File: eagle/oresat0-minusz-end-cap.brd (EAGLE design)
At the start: 106 x 106 mm, 30 parts, among them U1 LTC4305, U2 MMC5883MA, U3 MMC5883MA

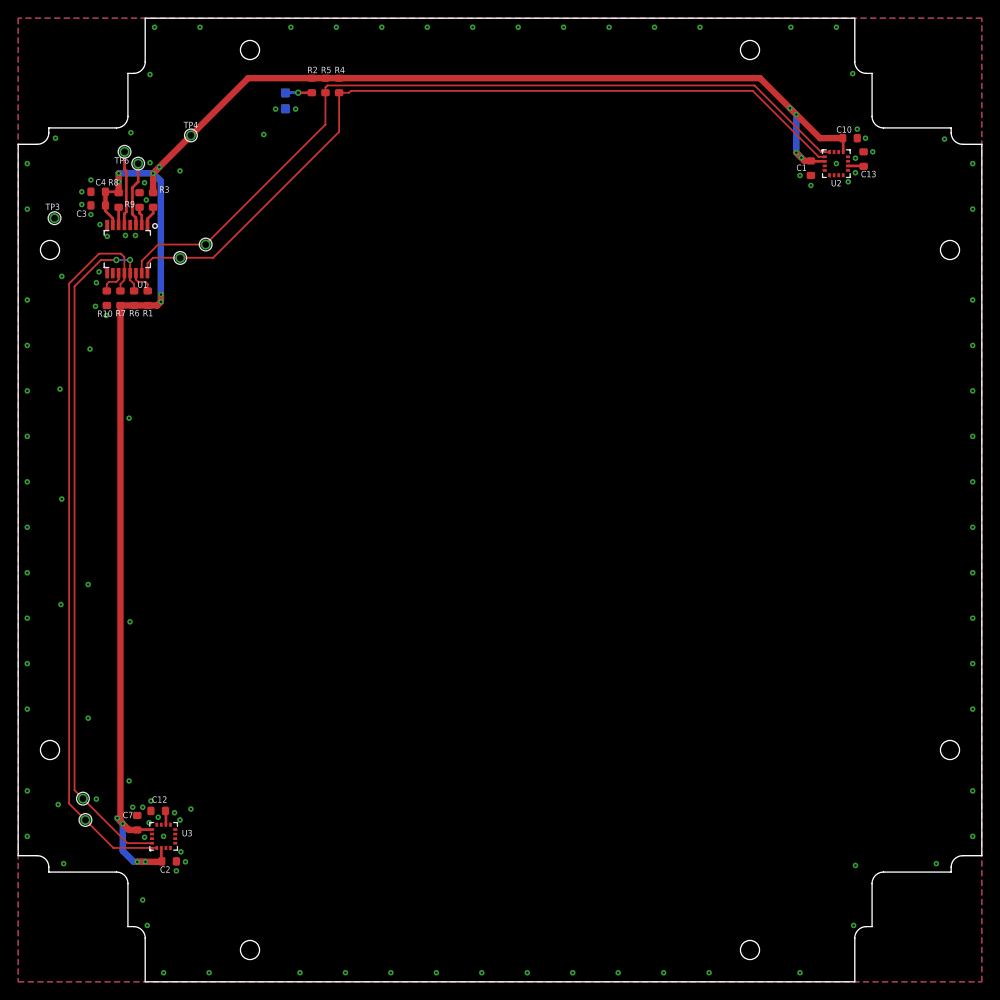
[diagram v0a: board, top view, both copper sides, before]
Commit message: Added connector to backplane. Added NP resistors connecting magnetometer interrupts to i2c buffer alert inputs. Moved traces out of bstop area, and moved components away from the backplane. Changed bus buffer i2c address. Added ground plane stitching, and fixed sharp edges on board outline.
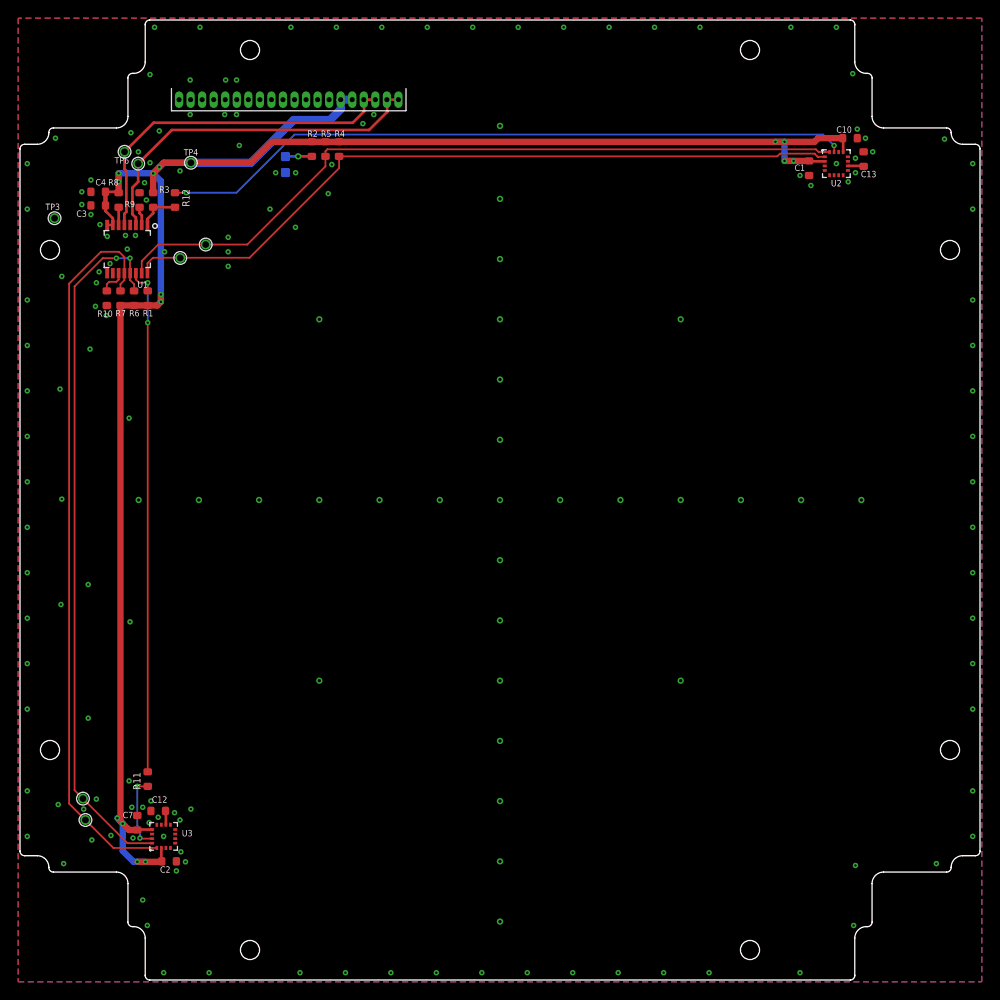
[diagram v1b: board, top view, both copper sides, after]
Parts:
- added J1: 6-104178-1, J-TE-6-104178-1-1.27mm-male-th:6-104178-1
- added R11, R12: NP, oresat-rcl:.0603-B-NOSILK
- moved D2 7.00 mm to (29.4, 89.9)
- moved R2 7.00 mm to (32.3, 91.6)
- moved R4 7.00 mm to (35.3, 91.6)
- moved R5 7.00 mm to (33.8, 91.6)
- moved TP4 3.00 mm to (19.0, 90.1)
- moved C1 0.20 mm to (87.0, 89.5)
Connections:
- new net !SD: J1.1
- new net CAN1_H: J1.4
- new net CAN1_L: J1.3
- new net CAN2_H: J1.9
- new net CAN2_L: J1.8
- new net N$10: R12.1, U2.15
- new net N$8: R11.1, U3.15
- new net OPD_PWR: J1.10
- new net OPD_SCL: J1.11
- new net OPD_SDA: J1.12
- new net SPARE1-TURNSTYLE-DPLY: J1.13
- new net SPARE2: J1.14
- new net VBUS: J1.7
- net 3.3V: now also J1.15, J1.16, U1.8
- net GND: now also J1.2, J1.5, J1.6; no longer U1.8
- net I2C-SCL: now also J1.17, J1.18
- net I2C-SDA: now also J1.19, J1.20
- net N$3: now also R11.2
- net N$4: now also R12.2
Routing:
- net N$10: track 0.00 -> 76.4 mm, vias 0 -> 2
- net N$3: track 2.95 -> 56.8 mm, vias 0 -> 2
- net I2C-SDA: track 7.16 -> 39.5 mm
- net I2C-SCL: track 8.22 -> 39.0 mm
- net 3.3V: track 201.0 -> 220.2 mm
- net N$8: track 0.00 -> 8.32 mm, vias 0 -> 2
- net SCL2: track 89.0 -> 81.5 mm
- net SDA2: track 90.5 -> 83.2 mm
- net N$4: track 2.21 -> 4.61 mm
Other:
- board size 106 x 106 mm -> 105.6 x 105.6 mm

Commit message: v1.0 end caps for OreSat0!
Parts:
- added TP10, TP11, TP12, TP13, TP14, TP15, TP16, TP17, TP18, TP19, TP9: TEST-POINT-LARGE-SQUARE, oresat-misc:1X01
- moved C1 0.28 mm to (86.8, 89.3)
- moved C10 0.28 mm to (91.3, 92.6)
- moved C13 0.28 mm to (92.8, 90.3)
- moved U2 0.28 mm to (89.8, 89.8)
- moved C3 0.28 mm to (8.60, 85.2)
- moved C4 0.28 mm to (8.60, 86.7)
- moved R8 0.28 mm to (10.8, 85.8)
- moved TP3 0.28 mm to (3.80, 83.8)
- moved C2 0.28 mm to (16.4, 13.1)
- moved D2 0.28 mm to (29.2, 89.7)
- moved R1 0.28 mm to (14.1, 75.0)
- moved R10 0.28 mm to (9.55, 75.0)
- moved R12 0.28 mm to (17.1, 85.8)
- moved R3 0.28 mm to (14.7, 85.8)
- moved R6 0.28 mm to (12.6, 75.0)
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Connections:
- net !SD: now also TP9.1
- net CAN1_H: now also TP11.1
- net CAN1_L: now also TP10.1
- net CAN2_H: now also TP14.1
- net CAN2_L: now also TP13.1
- net OPD_PWR: now also TP15.1
- net OPD_SCL: now also TP16.1
- net OPD_SDA: now also TP17.1
- net SPARE1-TURNSTYLE-DPLY: now also TP18.1
- net SPARE2: now also TP19.1
- net VBUS: now also TP12.1
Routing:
- net SPARE2: track 0.00 -> 3.22 mm
- net SPARE1-TURNSTYLE-DPLY: track 0.00 -> 3.12 mm
- net OPD_SDA: track 0.00 -> 3.03 mm
- net OPD_SCL: track 0.00 -> 2.93 mm
- net OPD_PWR: track 0.00 -> 2.84 mm
- net CAN2_H: track 0.00 -> 2.74 mm
- net CAN1_H: track 0.00 -> 2.68 mm
- net VBUS: track 0.00 -> 2.65 mm
- net CAN2_L: track 0.00 -> 2.65 mm
- net CAN1_L: track 0.00 -> 2.61 mm
- net !SD: track 0.00 -> 2.60 mm
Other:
- board size 105.6 x 105.6 mm -> 105.4 x 105.4 mm
- board text added: "!SD"
- board text added: "2020/8/28"
- board text added: "CAN1_H"
- board text added: "CAN1_L"
- board text added: "CAN2_H"
- board text added: "CAN2_L"
- board text added: "OPD_PWR"
- board text added: "OPD_SCL"
- board text added: "OPD_SDA"
- board text added: "SPARE2"
- board text added: "TURNSTILE"
- board text added: "VBUS"
- board text removed: "2020/8/24"

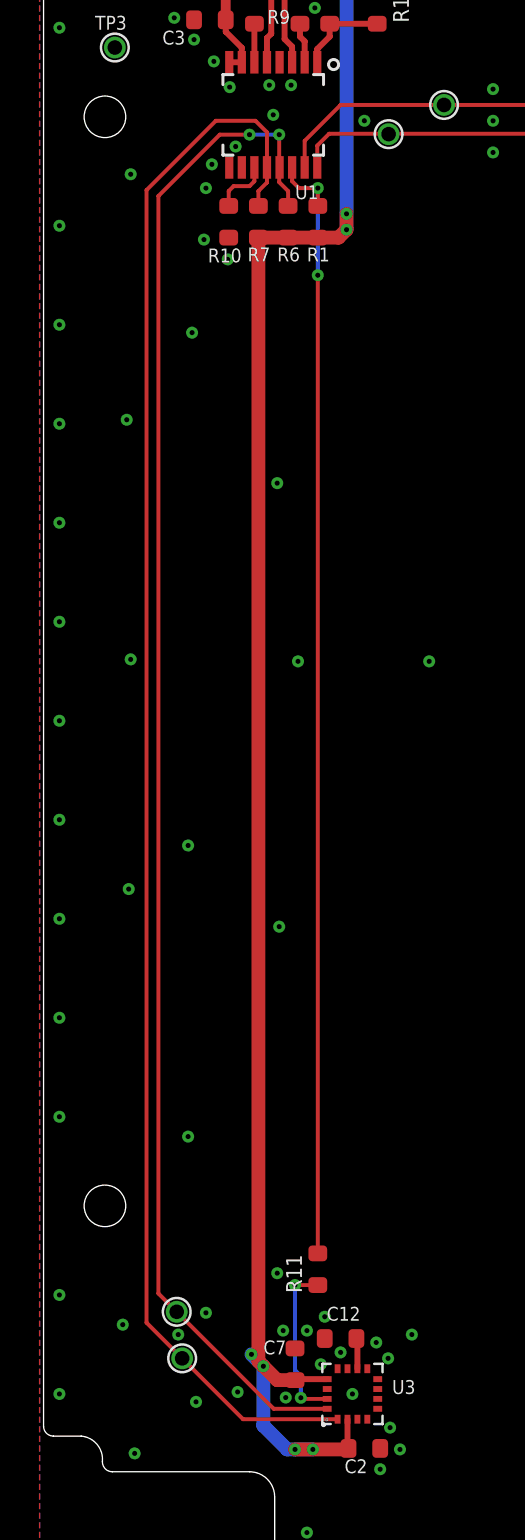
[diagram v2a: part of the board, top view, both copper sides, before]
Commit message: Moved SCL1 and SDA1 traces to avoid tstop area.
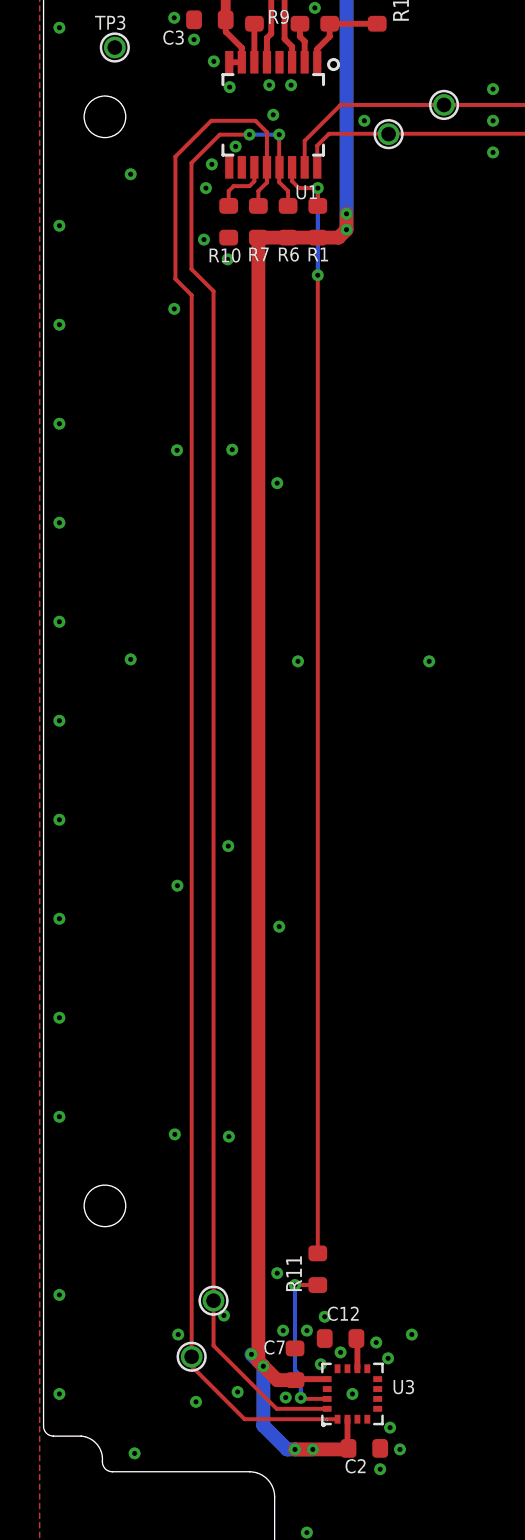
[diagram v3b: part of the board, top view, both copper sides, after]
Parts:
- moved TP5 1.94 mm to (8.79, 20.5)
- moved TP2 0.49 mm to (7.68, 17.7)
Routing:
- net SDA1: track 77.5 -> 76.1 mm
- net SCL1: track 80.5 -> 79.4 mm
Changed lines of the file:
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@@
 <?xml version="1.0" encoding="utf-8"?>
 <!DOCTYPE eagle SYSTEM "eagle.dtd">
-<eagle version="9.6.1">
+<eagle version="9.5.1">
 <drawing>
 <settings>
@@
 <attribute name="VALUE" x="11.15" y="73.8" size="0.8" layer="27" font="vector" ratio="15" rot="R90"/>
 </element>
-<element name="TP2" library="oresat-misc" package="1X01" value="TEST-POINT-LARGE-SQUARE" x="7.2" y="17.6" smashed="yes">
-<attribute name="NAME" x="6.4" y="16" size="0.635" layer="25" font="vector" ratio="20"/>
-<attribute name="NAME" x="8.2" y="15.9" size="0.635" layer="26" font="vector" ratio="20" rot="MR0"/>
-</element>
-<element name="TP5" library="oresat-misc" package="1X01" value="TEST-POINT-LARGE-SQUARE" x="6.925" y="19.95" smashed="yes">
-<attribute name="NAME" x="6.225" y="20.85" size="0.635" layer="25" font="vector" ratio="20"/>
-<attribute name="NAME" x="7.925" y="18.25" size="0.635" layer="26" font="vector" ratio="20" rot="MR0"/>
+<element name="TP2" library="oresat-misc" package="1X01" value="TEST-POINT-LARGE-SQUARE" x="7.68" y="17.68" smashed="yes">
+<attribute name="NAME" x="6.88" y="16.08" size="0.635" layer="25" font="vector" ratio="20"/>
+<attribute name="NAME" x="8.68" y="15.98" size="0.635" layer="26" font="vector" ratio="20" rot="MR0"/>
+</element>
+<element name="TP5" library="oresat-misc" package="1X01" value="TEST-POINT-LARGE-SQUARE" x="8.785" y="20.51" smashed="yes">
+<attribute name="NAME" x="8.085" y="21.41" size="0.635" layer="25" font="vector" ratio="20"/>
+<attribute name="NAME" x="9.785" y="18.81" size="0.635" layer="26" font="vector" ratio="20" rot="MR0"/>
 </element>
 <element name="TP7" library="oresat-misc" package="1X01" value="TEST-POINT-LARGE-SQUARE" x="17.625" y="79.425" smashed="yes">
@@
 <via x="18.2" y="13" extent="1-16" drill="0.254"/>
 <via x="91.9" y="12.6" extent="1-16" drill="0.254"/>
-<via x="7.5" y="28.8" extent="1-16" drill="0.254"/>
+<via x="9.56" y="28.8" extent="1-16" drill="0.254"/>
 <contactref element="C4" pad="2"/>
 <via x="12.7" y="81.9" extent="1-16" drill="0.254"/>
@@
 <via x="15.2" y="17.9" extent="1-16" drill="0.254"/>
 <via x="12.43" y="15.62" extent="1-16" drill="0.254"/>
-<via x="8.4" y="19.9" extent="1-16" drill="0.254"/>
+<via x="9.31" y="19.76" extent="1-16" drill="0.254"/>
 <via x="9.5" y="73.1" extent="1-16" drill="0.254"/>
 <via x="8.3" y="74.1" extent="1-16" drill="0.254"/>
@@
 <via x="7.8" y="88" extent="1-16" drill="0.254"/>
 <via x="4.6" y="77.4" extent="1-16" drill="0.254"/>
-<via x="4.4" y="65" extent="1-16" drill="0.254"/>
+<via x="6.94" y="63.46" extent="1-16" drill="0.254"/>
 <via x="4.6" y="52.9" extent="1-16" drill="0.254"/>
-<via x="4.5" y="41.3" extent="1-16" drill="0.254"/>
-<via x="4.2" y="19.3" extent="1-16" drill="0.254"/>
-<via x="7.5" y="43.5" extent="1-16" drill="0.254"/>
-<via x="7.7" y="69.4" extent="1-16" drill="0.254"/>
+<via x="6.96" y="41.47" extent="1-16" drill="0.254"/>
+<via x="6.83" y="28.91" extent="1-16" drill="0.254"/>
+<via x="9.53" y="43.47" extent="1-16" drill="0.254"/>
+<via x="6.8" y="70.6" extent="1-16" drill="0.254"/>
 <via x="12" y="21.9" extent="1-16" drill="0.254"/>
 <via x="12.1" y="39.4" extent="1-16" drill="0.254"/>
@@
 <via x="7.9" y="15.4" extent="1-16" drill="0.254"/>
 <via x="7" y="18.8" extent="1-16" drill="0.254"/>
+<via x="9.73" y="63.49" extent="1-16" drill="0.254"/>
 </signal>
 <signal name="N$262">
@@
 <via x="10.6" y="79.4" extent="1-16" drill="0.254"/>
 <wire x1="10.6" y1="79.4" x2="9.1" y2="79.4" width="0.2" layer="1"/>
-<wire x1="6" y1="76.3" x2="9.1" y2="79.4" width="0.2" layer="1"/>
+<wire x1="7.67" y1="77.97" x2="9.1" y2="79.4" width="0.2" layer="1"/>
 <wire x1="12.1" y1="79.4" x2="10.6" y2="79.4" width="0.2" layer="16"/>
 <contactref element="TP5" pad="1"/>
-<wire x1="11.825" y1="15.05" x2="6.925" y2="19.95" width="0.2" layer="1"/>
-<wire x1="14.525" y1="15.05" x2="11.825" y2="15.05" width="0.2" layer="1"/>
-<wire x1="6.925" y1="19.95" x2="6" y2="20.875" width="0.2" layer="1"/>
-<wire x1="6" y1="20.875" x2="6" y2="76.3" width="0.2" layer="1"/>
+<wire x1="11.975" y1="15.05" x2="8.785" y2="18.24" width="0.2" layer="1"/>
+<wire x1="8.785" y1="18.24" x2="8.785" y2="20.51" width="0.2" layer="1"/>
+<wire x1="14.525" y1="15.05" x2="11.975" y2="15.05" width="0.2" layer="1"/>
+<wire x1="8.785" y1="20.51" x2="8.785" y2="71.49" width="0.2" layer="1"/>
+<wire x1="8.785" y1="71.49" x2="7.67" y2="72.605" width="0.2" layer="1"/>
+<wire x1="7.67" y1="72.605" x2="7.67" y2="77.97" width="0.2" layer="1"/>
 </signal>
 <signal name="SCL1">
@@
 <wire x1="11.05" y1="76.55" x2="11.4825" y2="76.9825" width="0.2" layer="1"/>
 <wire x1="11.4825" y1="79.5175" x2="11.4825" y2="77.7457" width="0.2" layer="1"/>
-<wire x1="5.4" y1="76.6" x2="8.9" y2="80.1" width="0.2" layer="1"/>
-<wire x1="8.9" y1="80.1" x2="10.9" y2="80.1" width="0.2" layer="1"/>
+<wire x1="6.86" y1="78.29" x2="8.67" y2="80.1" width="0.2" layer="1"/>
+<wire x1="8.67" y1="80.1" x2="10.9" y2="80.1" width="0.2" layer="1"/>
 <wire x1="10.9" y1="80.1" x2="11.4825" y2="79.5175" width="0.2" layer="1"/>
 <contactref element="TP2" pad="1"/>
-<wire x1="10.275" y1="14.525" x2="7.2" y2="17.6" width="0.2" layer="1"/>
-<wire x1="15.05" y1="14.525" x2="10.275" y2="14.525" width="0.2" layer="1"/>
-<wire x1="7.2" y1="17.6" x2="5.4" y2="19.4" width="0.2" layer="1"/>
-<wire x1="5.4" y1="19.4" x2="5.4" y2="76.6" width="0.2" layer="1"/>
+<wire x1="10.355" y1="14.525" x2="7.68" y2="17.2" width="0.2" layer="1"/>
+<wire x1="7.68" y1="17.2" x2="7.68" y2="17.68" width="0.2" layer="1"/>
+<wire x1="15.05" y1="14.525" x2="10.355" y2="14.525" width="0.2" layer="1"/>
+<wire x1="7.68" y1="17.68" x2="7.68" y2="71.29" width="0.2" layer="1"/>
+<wire x1="7.68" y1="71.29" x2="6.86" y2="72.11" width="0.2" layer="1"/>
+<wire x1="6.86" y1="72.11" x2="6.86" y2="78.29" width="0.2" layer="1"/>
 </signal>
 <signal name="I2C-SDA">

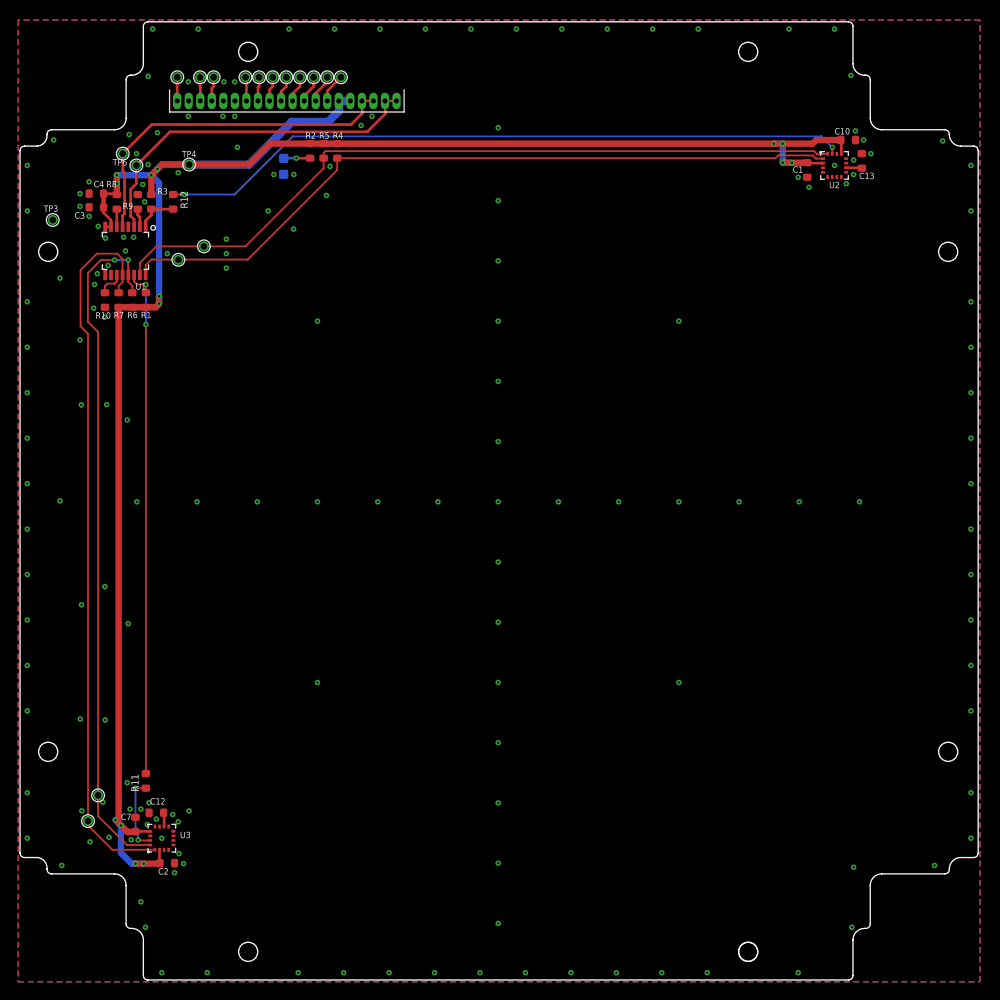
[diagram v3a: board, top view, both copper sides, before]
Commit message: Updated DXF and board outline. Also cleaned up tNames and Bplace layers around backplane connector.
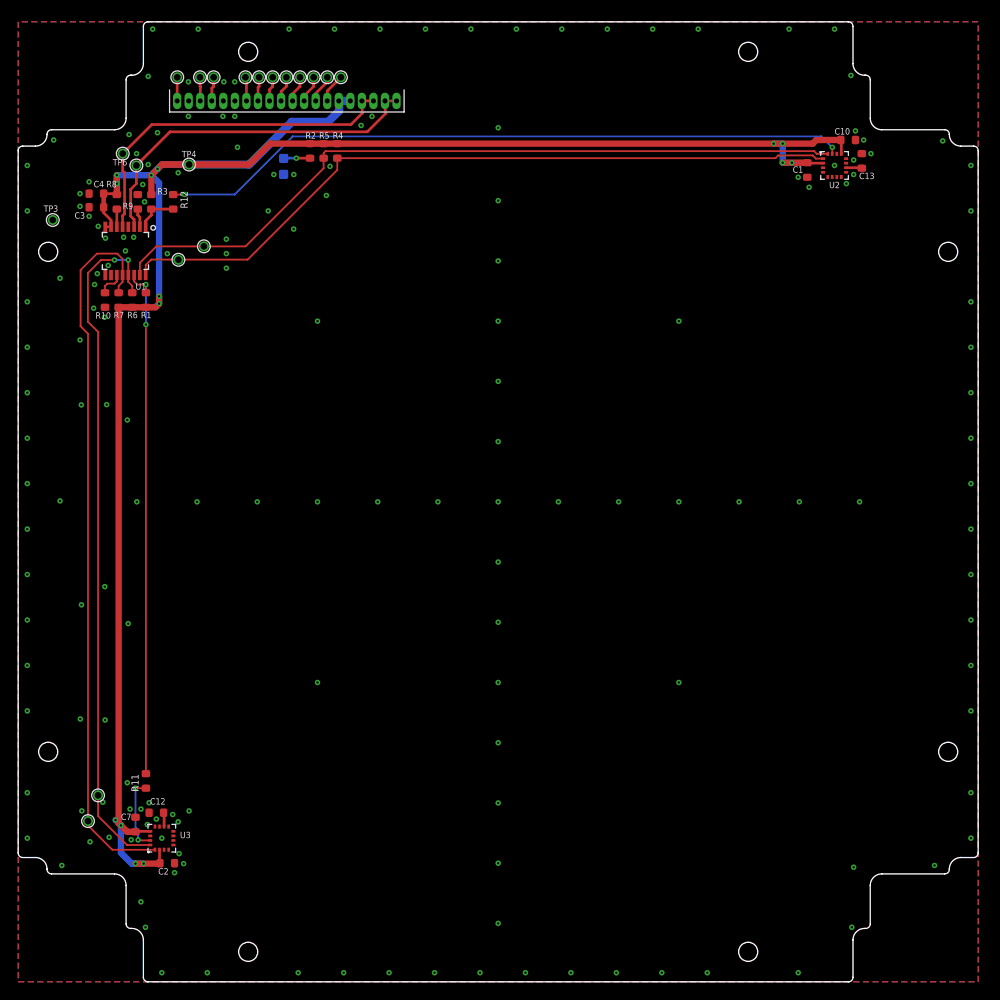
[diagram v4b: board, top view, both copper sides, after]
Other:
- board size 105.4 x 105.4 mm -> 105.6 x 105.6 mm
